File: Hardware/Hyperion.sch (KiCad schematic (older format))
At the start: 1 part, among them J1 CUBESAT-BUS

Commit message: Add core components
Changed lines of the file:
@@
 LIBS:power
 LIBS:Aerodyne_v2
-EELAYER 24 0
+LIBS:Hyperion-cache
+EELAYER 27 0
 EELAYER END
 $Descr A4 11693 8268
 encoding utf-8
-Sheet 1 1
+Sheet 1 2
 Title ""
-Date ""
+Date "11 oct 2013"
 Rev ""
 Comp ""
@@
 	1    0    0    -1
 $EndComp
+$Sheet
+S 5500 1700 1000 1000
+U 525790DA
+F0 "Core" 50
+F1 "Core.sch" 50
+$EndSheet
 $EndSCHEMATC

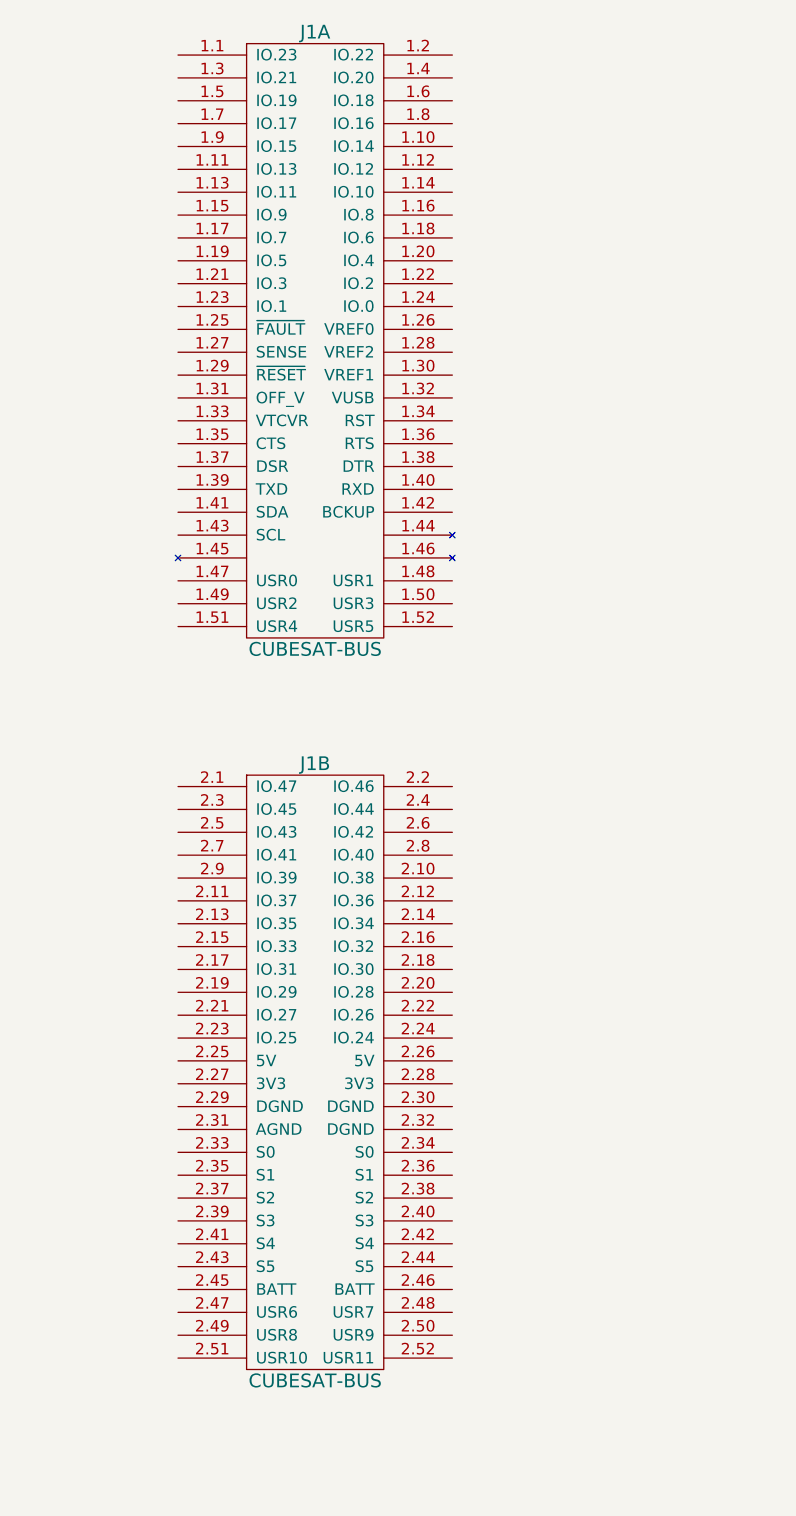
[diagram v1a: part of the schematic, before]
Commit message: Add bus pinout
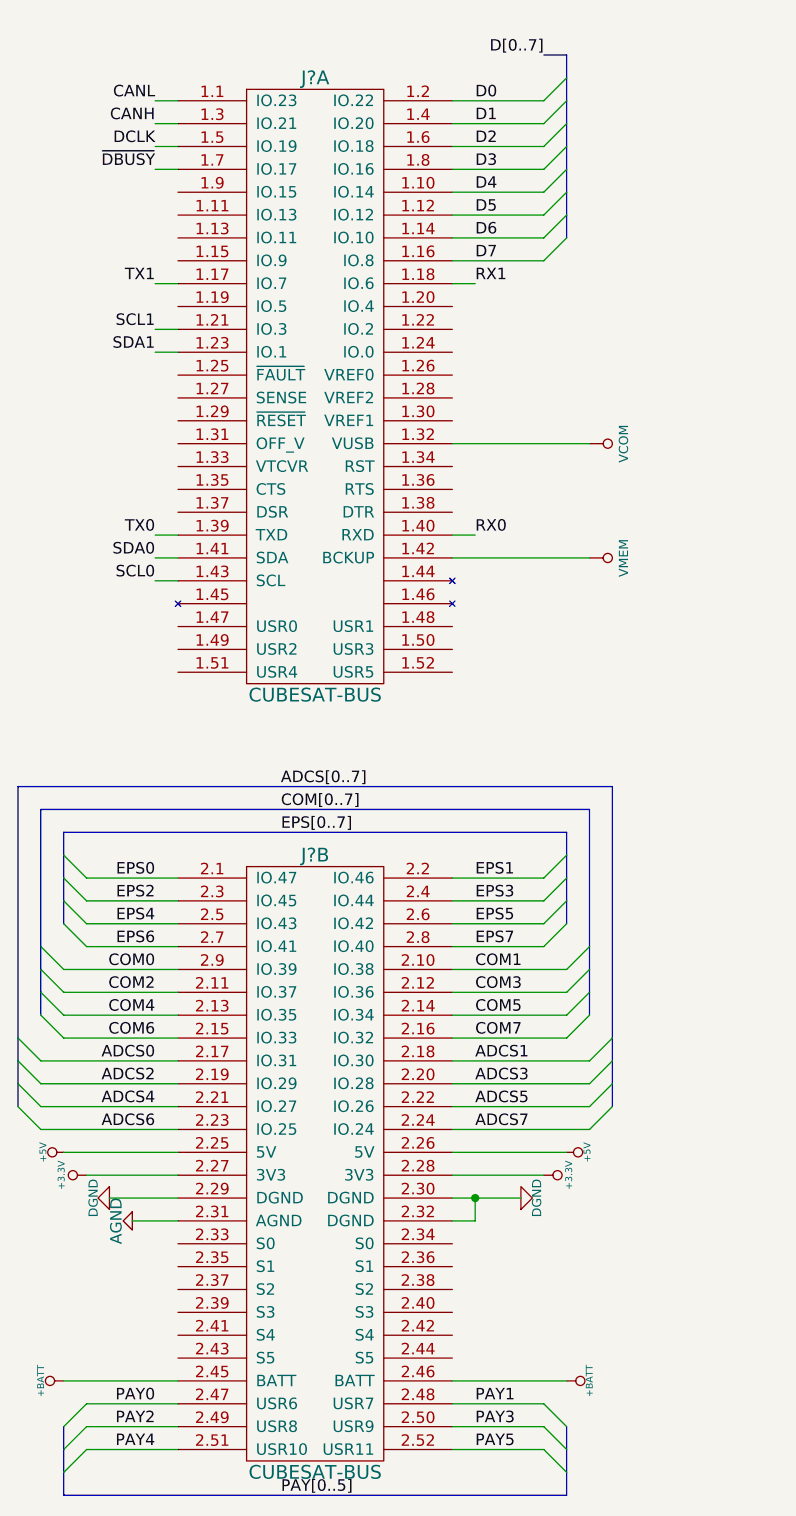
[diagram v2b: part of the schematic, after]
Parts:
- renumbered J1 to J?
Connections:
- net CANL: now reaches J?.1.1 (IO.23)
- net D4: now reaches J?.1.10 (IO.14)
- net D5: now reaches J?.1.12 (IO.12)
- net D6: now reaches J?.1.14 (IO.10)
- net D7: now reaches J?.1.16 (IO.8)
- net TX1: now reaches J?.1.17 (IO.7)
- net RX1: now reaches J?.1.18 (IO.6)
- net D0: now reaches J?.1.2 (IO.22)
- net SCL1: now reaches J?.1.21 (IO.3)
- net SDA1: now reaches J?.1.23 (IO.1)
- net CANH: now reaches J?.1.3 (IO.21)
- net VCOM: now reaches J?.1.32 (VUSB)
- net TX0: now reaches J?.1.39 (TXD)
- net D1: now reaches J?.1.4 (IO.20)
- net RX0: now reaches J?.1.40 (RXD)
- net SDA0: now reaches J?.1.41 (SDA)
- net VMEM: now reaches J?.1.42 (BCKUP)
- net SCL0: now reaches J?.1.43 (SCL)
- net DCLK: now reaches J?.1.5 (IO.19)
- net D2: now reaches J?.1.6 (IO.18)
- net ~DBUSY: now reaches J?.1.7 (IO.17)
- net D3: now reaches J?.1.8 (IO.16)
- net EPS0: now reaches J?.2.1 (IO.47)
- net COM1: now reaches J?.2.10 (IO.38)
- net COM2: now reaches J?.2.11 (IO.37)
- net COM3: now reaches J?.2.12 (IO.36)
- net COM4: now reaches J?.2.13 (IO.35)
- net COM5: now reaches J?.2.14 (IO.34)
- net COM6: now reaches J?.2.15 (IO.33)
- net COM7: now reaches J?.2.16 (IO.32)
- net ADCS0: now reaches J?.2.17 (IO.31)
- net ADCS1: now reaches J?.2.18 (IO.30)
- net ADCS2: now reaches J?.2.19 (IO.29)
- net EPS1: now reaches J?.2.2 (IO.46)
- net ADCS3: now reaches J?.2.20 (IO.28)
- net ADCS4: now reaches J?.2.21 (IO.27)
- net ADCS5: now reaches J?.2.22 (IO.26)
- net ADCS6: now reaches J?.2.23 (IO.25)
- net ADCS7: now reaches J?.2.24 (IO.24)
- net +5V: now reaches J?.2.25 (5V)
- net +5V: now also J?.2.26 (5V)
- net +3.3V: now reaches J?.2.27 (3V3)
- net +3.3V: now also J?.2.28 (3V3)
- net DGND: now reaches J?.2.29 (DGND)
- net DGND: now also J?.2.30 (DGND), J?.2.32 (DGND)
- net EPS2: now reaches J?.2.3 (IO.45)
- net AGND: now reaches J?.2.31 (AGND)
- net EPS3: now reaches J?.2.4 (IO.44)
- net +BATT: now reaches J?.2.45 (BATT)
- net +BATT: now also J?.2.46 (BATT)
- net PAY0: now reaches J?.2.47 (USR6)
- net PAY1: now reaches J?.2.48 (USR7)
- net PAY2: now reaches J?.2.49 (USR8)
- net EPS4: now reaches J?.2.5 (IO.43)
- net PAY3: now reaches J?.2.50 (USR9)
- net PAY4: now reaches J?.2.51 (USR10)
- net PAY5: now reaches J?.2.52 (USR11)
- net EPS5: now reaches J?.2.6 (IO.42)
- net EPS6: now reaches J?.2.7 (IO.41)
- net EPS7: now reaches J?.2.8 (IO.40)
- net COM0: now reaches J?.2.9 (IO.39)
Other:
- moved on the sheet: J?A, J?B

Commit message: Save annotation
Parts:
- gave numbers to parts that had none: 1
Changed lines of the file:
@@
 $EndDescr
 $Comp
-L CUBESAT-BUS J?
+L CUBESAT-BUS J1
 U 1 1 5253906A
 P 2000 2350
-F 0 "J?" H 2000 3700 60  0000 C CNN
+F 0 "J1" H 2000 3700 60  0000 C CNN
 F 1 "CUBESAT-BUS" H 2000 1000 60  0000 C CNN
 F 2 "" H 2000 2350 60  0000 C CNN
@@
 $EndComp
 $Comp
-L CUBESAT-BUS J?
+L CUBESAT-BUS J1
 U 2 1 52539079
 P 2000 5750
-F 0 "J?" H 2000 7100 60  0000 C CNN
+F 0 "J1" H 2000 7100 60  0000 C CNN
 F 1 "CUBESAT-BUS" H 2000 4400 60  0000 C CNN
 F 2 "" H 2000 5750 60  0000 C CNN
@@
 D7
 $Comp
-L VMEM #PWR?
+L VMEM #PWR11
 U 1 1 52FF2E7C
 P 3200 3100
-F 0 "#PWR?" H 3200 3300 40  0001 C CNN
+F 0 "#PWR11" H 3200 3300 40  0001 C CNN
 F 1 "VMEM" H 3200 3250 40  0000 C CNN
 F 2 "" H 3200 3100 60  0000 C CNN
@@
 $EndComp
 $Comp
-L VCOM #PWR?
+L VCOM #PWR10
 U 1 1 52FF2EBE
 P 3200 2600
-F 0 "#PWR?" H 3200 2800 40  0001 C CNN
+F 0 "#PWR10" H 3200 2800 40  0001 C CNN
 F 1 "VCOM" H 3200 2750 40  0000 C CNN
 F 2 "" H 3200 2600 60  0000 C CNN
@@
 $EndComp
 $Comp
-L +5V #PWR?
+L +5V #PWR8
 U 1 1 52FF2F36
 P 3100 5700
-F 0 "#PWR?" H 3100 5790 20  0001 C CNN
+F 0 "#PWR8" H 3100 5790 20  0001 C CNN
 F 1 "+5V" H 3100 5790 30  0000 C CNN
 F 2 "" H 3100 5700 60  0000 C CNN
@@
 $EndComp
 $Comp
-L +5V #PWR?
+L +5V #PWR1
 U 1 1 52FF2F45
 P 900 5700
-F 0 "#PWR?" H 900 5790 20  0001 C CNN
+F 0 "#PWR1" H 900 5790 20  0001 C CNN
 F 1 "+5V" H 900 5790 30  0000 C CNN
 F 2 "" H 900 5700 60  0000 C CNN
@@
 $EndComp
 $Comp
-L +3.3V #PWR?
+L +3.3V #PWR3
 U 1 1 52FF2F54
 P 1000 5800
-F 0 "#PWR?" H 1000 5760 30  0001 C CNN
+F 0 "#PWR3" H 1000 5760 30  0001 C CNN
 F 1 "+3.3V" H 1000 5910 30  0000 C CNN
 F 2 "" H 1000 5800 60  0000 C CNN
@@
 $EndComp
 $Comp
-L +3.3V #PWR?
+L +3.3V #PWR7
 U 1 1 52FF2F63
 P 3000 5800
-F 0 "#PWR?" H 3000 5760 30  0001 C CNN
+F 0 "#PWR7" H 3000 5760 30  0001 C CNN
 F 1 "+3.3V" H 3000 5910 30  0000 C CNN
 F 2 "" H 3000 5800 60  0000 C CNN
@@
 $EndComp
 $Comp
-L DGND #PWR?
+L DGND #PWR4
 U 1 1 52FF2F72
 P 1100 5900
-F 0 "#PWR?" H 1100 5900 40  0001 C CNN
+F 0 "#PWR4" H 1100 5900 40  0001 C CNN
 F 1 "DGND" H 1100 5830 40  0000 C CNN
 F 2 "" H 1100 5900 60  0000 C CNN
@@
 $EndComp
 $Comp
-L DGND #PWR?
+L DGND #PWR6
 U 1 1 52FF2F81
 P 2900 5900
-F 0 "#PWR?" H 2900 5900 40  0001 C CNN
+F 0 "#PWR6" H 2900 5900 40  0001 C CNN
 F 1 "DGND" H 2900 5830 40  0000 C CNN
 F 2 "" H 2900 5900 60  0000 C CNN
@@
 $EndComp
 $Comp
-L +BATT #PWR?
+L +BATT #PWR9
 U 1 1 52FF2F9F
 P 3100 6700
-F 0 "#PWR?" H 3100 6650 20  0001 C CNN
+F 0 "#PWR9" H 3100 6650 20  0001 C CNN
 F 1 "+BATT" H 3100 6800 30  0000 C CNN
 F 2 "" H 3100 6700 60  0000 C CNN
@@
 $EndComp
 $Comp
-L +BATT #PWR?
+L +BATT #PWR2
 U 1 1 52FF2FAE
 P 900 6700
-F 0 "#PWR?" H 900 6650 20  0001 C CNN
+F 0 "#PWR2" H 900 6650 20  0001 C CNN
 F 1 "+BATT" H 900 6800 30  0000 C CNN
 F 2 "" H 900 6700 60  0000 C CNN
@@
 $EndComp
 $Comp
-L AGND #PWR?
+L AGND #PWR5
 U 1 1 52FF3031
 P 1200 6000
-F 0 "#PWR?" H 1200 6000 40  0001 C CNN
+F 0 "#PWR5" H 1200 6000 40  0001 C CNN
 F 1 "AGND" H 1200 5930 50  0000 C CNN
 F 2 "" H 1200 6000 60  0000 C CNN
@@
 	2600 5800 3000 5800
 Wire Wire Line
-	2600 5900 2700 5900
-Wire Wire Line
-	2700 5900 2900 5900
+	2600 5900 2900 5900
 Wire Wire Line
 	3100 6700 2600 6700
@@
 	1400 6700 900  6700
 Wire Bus Line
-	900  4300 900  4400
-Wire Bus Line
-	900  4400 900  4500
-Wire Bus Line
-	900  4500 900  4600
-Wire Bus Line
-	900  4600 900  4700
+	900  4300 900  4700
 Wire Bus Line
 	900  4300 3100 4300
 Wire Bus Line
-	3100 4300 3100 4400
-Wire Bus Line
-	3100 4400 3100 4500
-Wire Bus Line
-	3100 4500 3100 4600
-Wire Bus Line
-	3100 4600 3100 4700
-Wire Bus Line
-	800  4200 800  4800
-Wire Bus Line
-	800  4800 800  4900
-Wire Bus Line
-	800  4900 800  5000
-Wire Bus Line
-	800  5000 800  5100
+	3100 4300 3100 4700
+Wire Bus Line
+	800  4200 800  5100
 Wire Bus Line
 	800  4200 3200 4200
 Wire Bus Line
-	3200 4200 3200 4800
-Wire Bus Line
-	3200 4800 3200 4900
-Wire Bus Line
-	3200 4900 3200 5000
-Wire Bus Line
-	3200 5000 3200 5100
-Wire Bus Line
-	700  4100 700  5200
-Wire Bus Line
-	700  5200 700  5300
-Wire Bus Line
-	700  5300 700  5400
-Wire Bus Line
-	700  5400 700  5500
+	3200 4200 3200 5100
+Wire Bus Line
+	700  4100 700  5500
 Wire Bus Line
 	700  4100 3300 4100
 Wire Bus Line
-	3300 4100 3300 5200
-Wire Bus Line
-	3300 5200 3300 5300
-Wire Bus Line
-	3300 5300 3300 5400
-Wire Bus Line
-	3300 5400 3300 5500
-Wire Bus Line
-	900  6900 900  7000
-Wire Bus Line
-	900  7000 900  7100
-Wire Bus Line
-	900  7100 900  7200
-Wire Bus Line
-	3100 7200 3100 7100
-Wire Bus Line
-	3100 7100 3100 7000
-Wire Bus Line
-	3100 7000 3100 6900
+	3300 4100 3300 5500
+Wire Bus Line
+	900  6900 900  7200
+Wire Bus Line
+	3100 6900 3100 7200
 Wire Wire Line
 	2600 6000 2700 6000
@@
 Connection ~ 2700 5900
 Wire Bus Line
-	900  7200 3100 7200
+	3100 7200 900  7200
 Entry Wire Line
 	3000 1100 3100 1000
@@
 	3000 1800 3100 1700
 Wire Bus Line
-	3100 1700 3100 1600
-Wire Bus Line
-	3100 1600 3100 1500
-Wire Bus Line
-	3100 1500 3100 1400
-Wire Bus Line
-	3100 1400 3100 1300
-Wire Bus Line
-	3100 1300 3100 1200
-Wire Bus Line
-	3100 1200 3100 1100
-Wire Bus Line
-	3100 1100 3100 1000
-Wire Bus Line
-	3100 1000 3100 900
+	3100 900  3100 1700
 Wire Bus Line
 	3100 900  3000 900

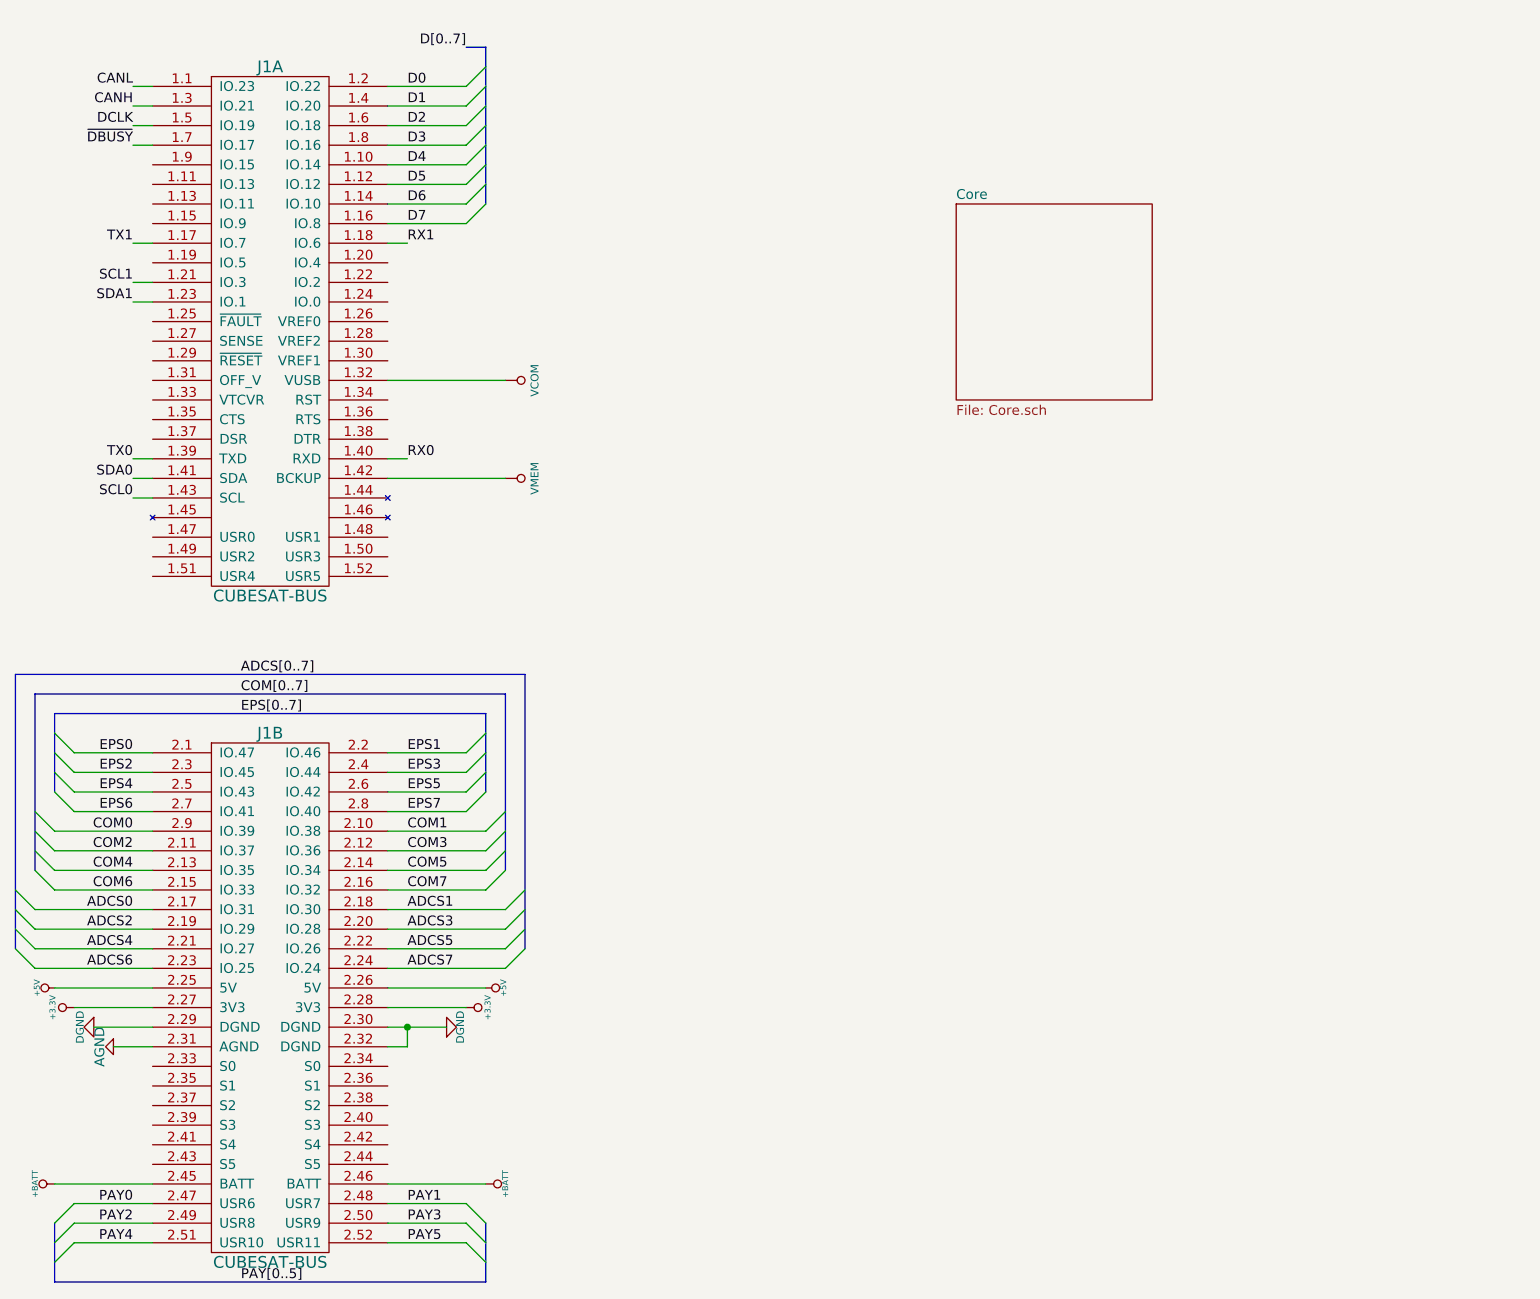
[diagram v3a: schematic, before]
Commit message: Add dual channel FTDI
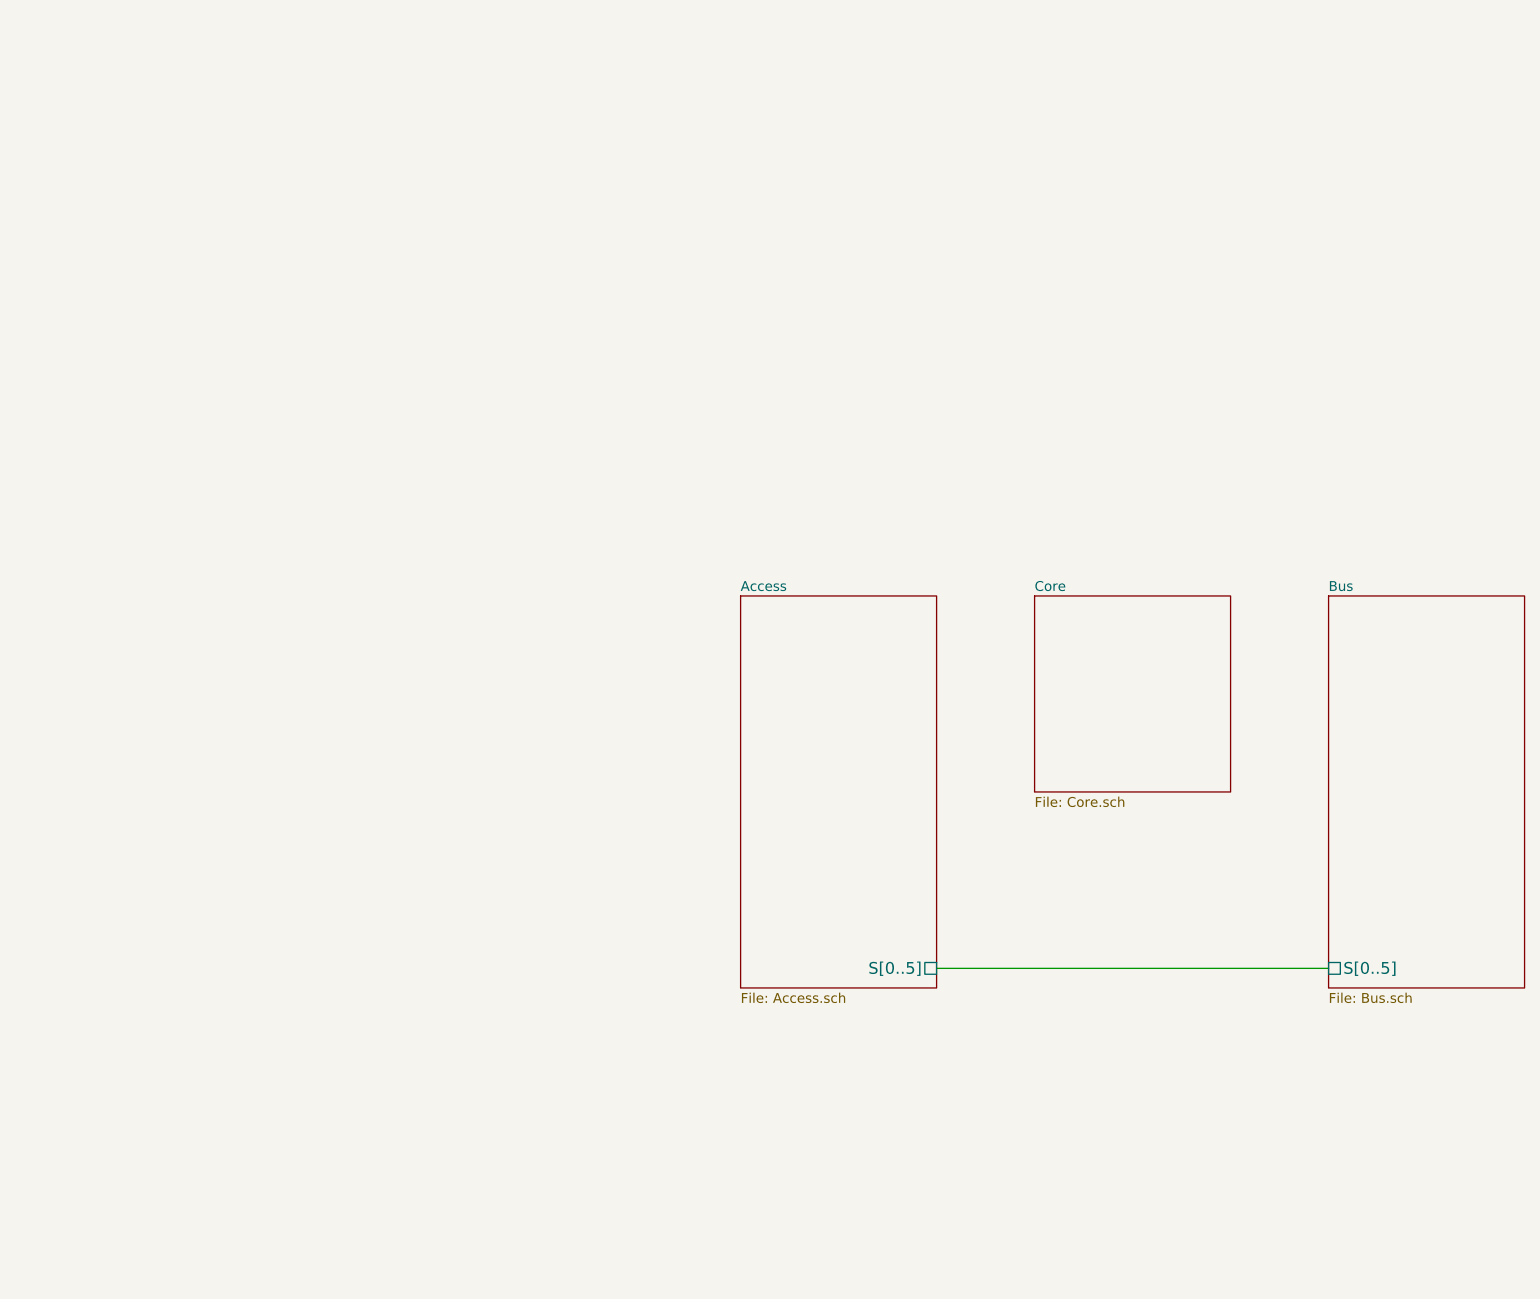
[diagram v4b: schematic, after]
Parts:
- removed J1: CUBESAT-BUS, symbol CUBESAT-BUS
